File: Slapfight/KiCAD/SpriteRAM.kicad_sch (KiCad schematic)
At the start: 24 parts, among them U1N_ 74LS00, U1P_ 74LS393, U1Q_ 74LS393, U2K_ 74LS32, U2L RAM_2016, U3K 74LS245

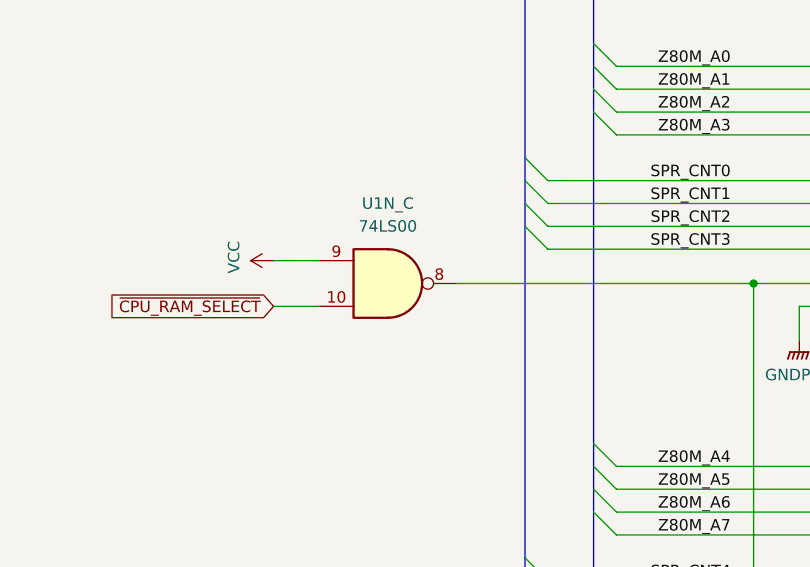
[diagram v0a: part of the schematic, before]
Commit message: Component naming updates
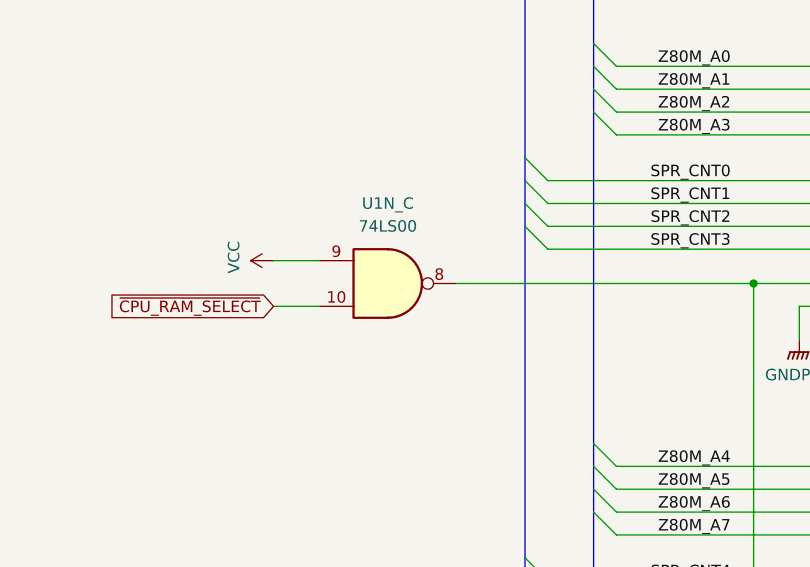
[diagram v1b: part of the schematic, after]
